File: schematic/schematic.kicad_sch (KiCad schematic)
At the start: 7 parts, among them M1 Stepper_Motor_bipolar, M2 Stepper_Motor_bipolar, U1 module_mpu6050

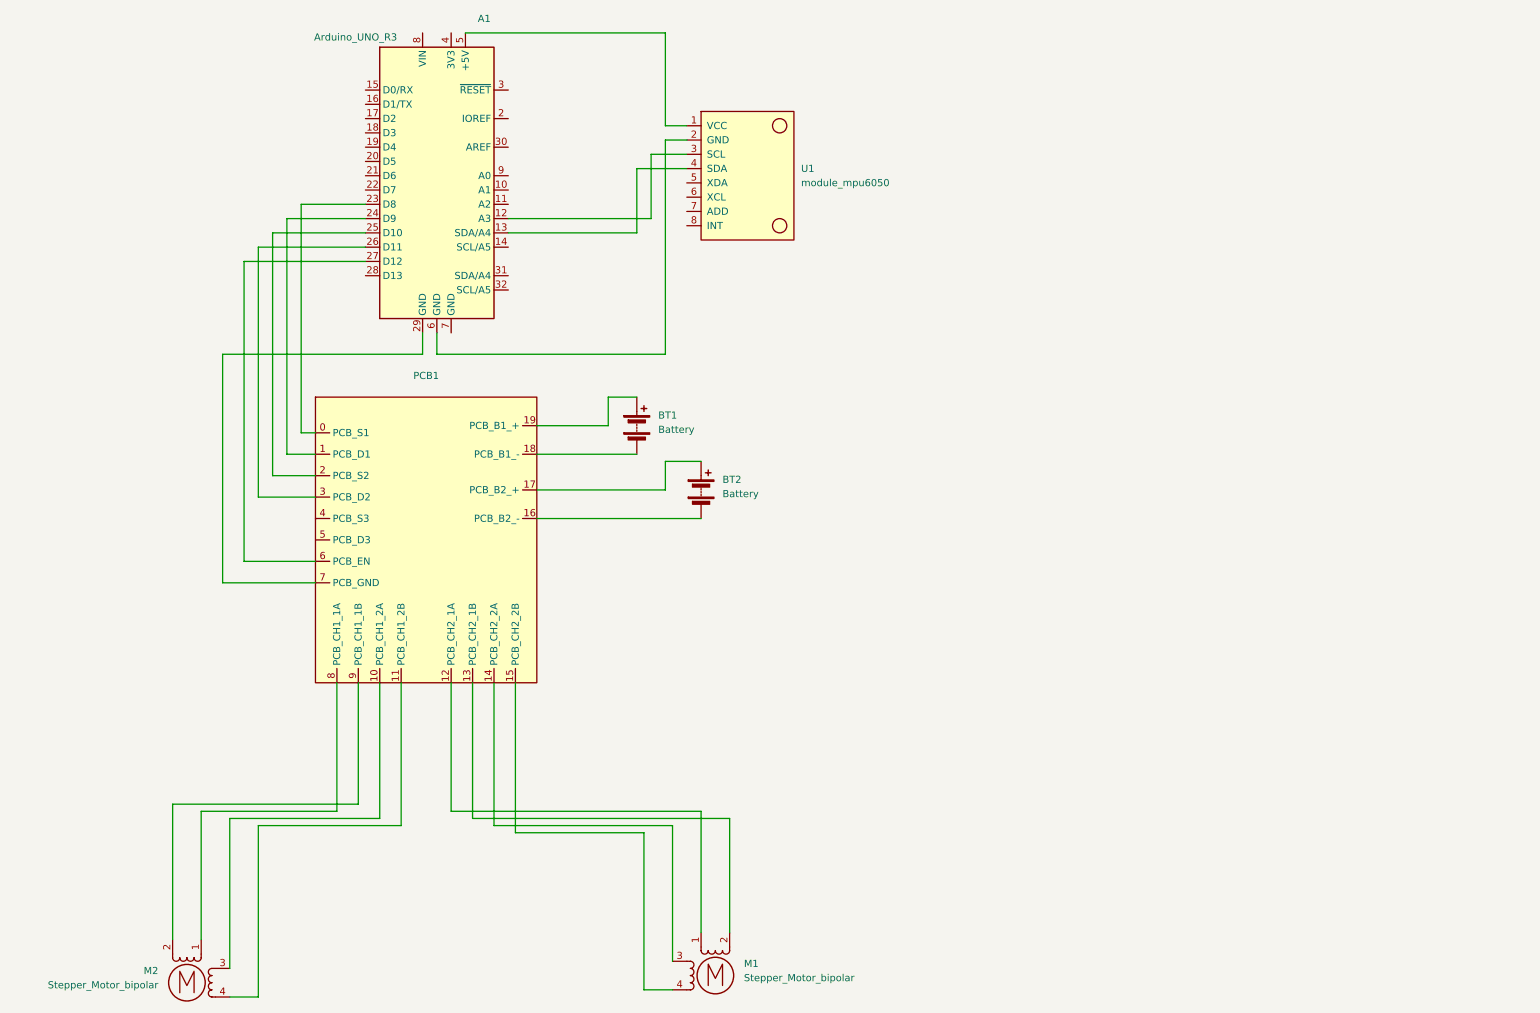
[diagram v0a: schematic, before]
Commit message: Fix MPU6050 pins to Digital pins: D3=SCL, D4=SDA not A3=SCL and A4=SDA
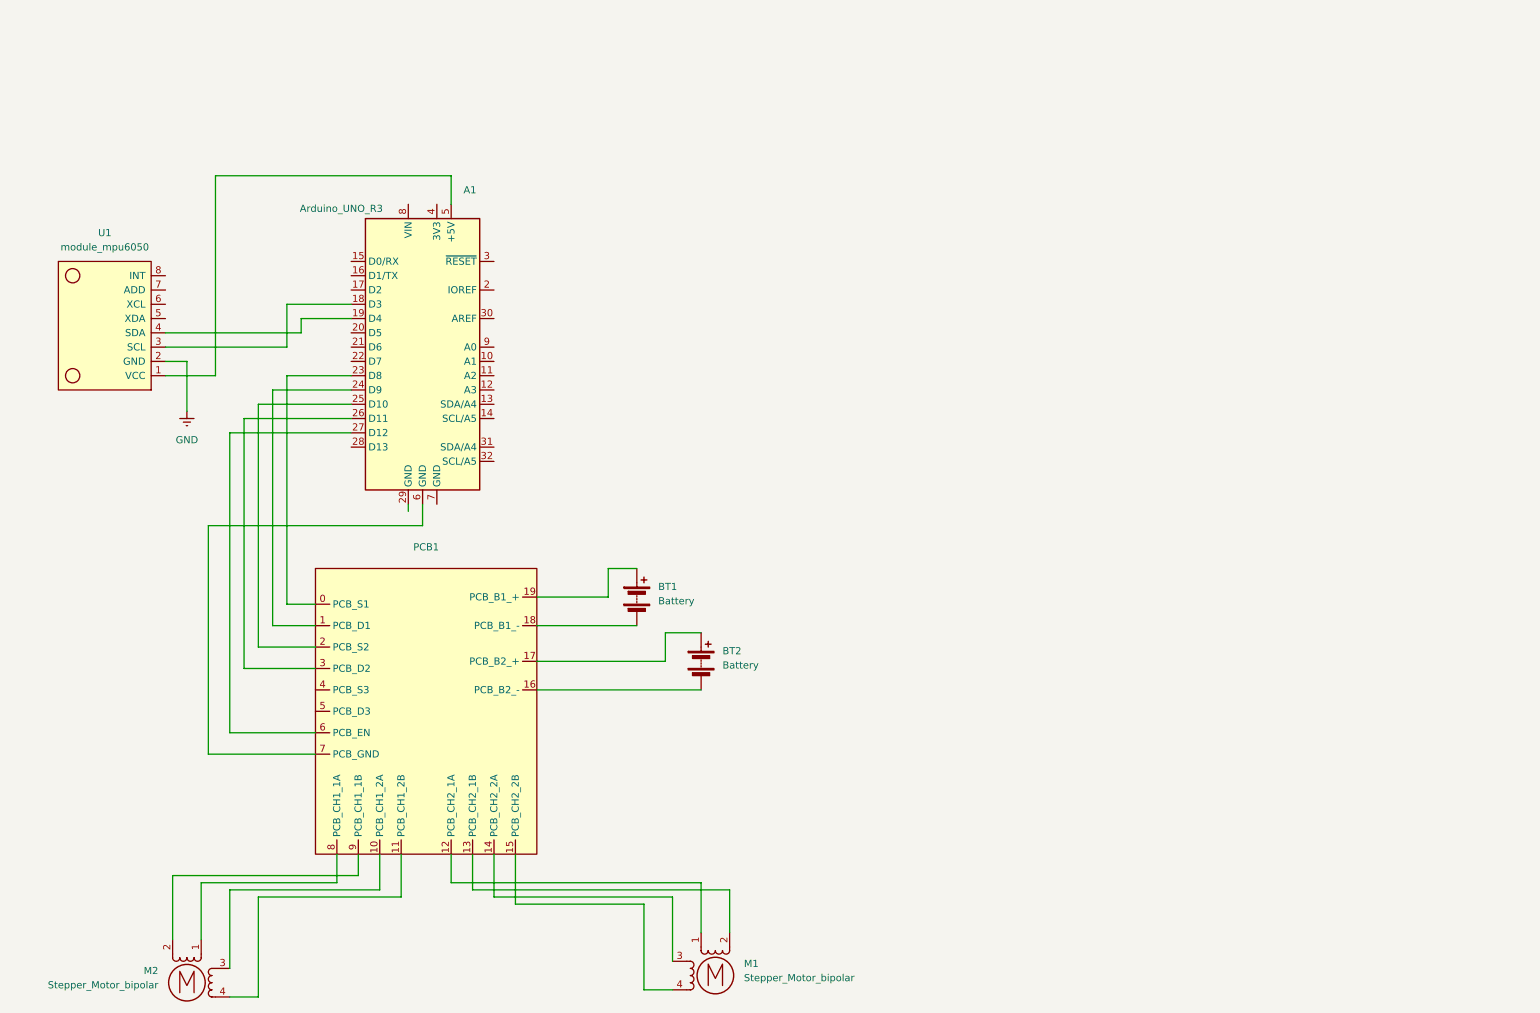
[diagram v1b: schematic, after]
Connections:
- net at PCB1.7 (PCB_GND): now also A1.6 (GND); no longer A1.29 (GND)
- net GND: now reaches U1.2 (GND)
- net GND: no longer A1.6 (GND)
- net at U1.3 (SCL): now also A1.18 (D3); no longer A1.12 (A3)
- net at U1.4 (SDA): now also A1.19 (D4); no longer A1.13 (SDA/A4)
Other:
- moved on the sheet: A1, BT1, BT2, PCB1, U1

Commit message: completed schematic (#19)
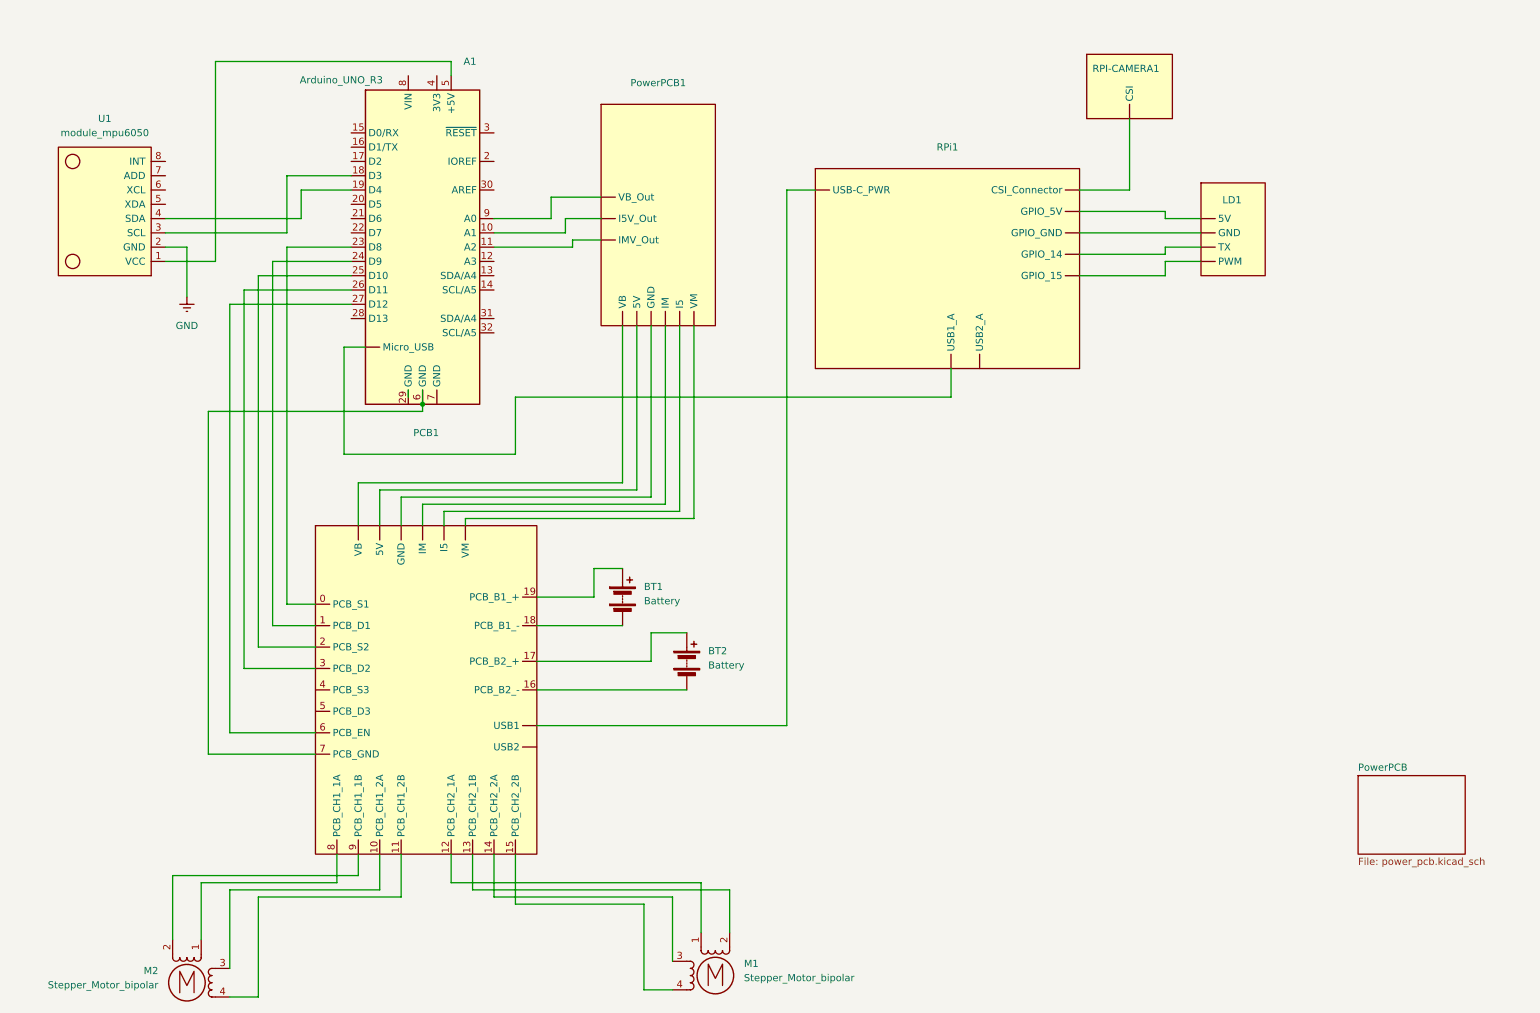
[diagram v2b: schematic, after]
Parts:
- added LD1: ~, symbol BalanceBotSymbolLibrary:LD06
- added PowerPCB1: ~, symbol BalanceBotSymbolLibrary:PowerPCB
- added RPI-CAMERA1: ~, symbol BalanceBotSymbolLibrary:Camera_Module_v2
- added RPi1: ~, symbol BalanceBotSymbolLibrary:RPi4
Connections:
- net at A1.10 (A1): now also PowerPCB1. (VM)
- net at A1.11 (A2): now also PowerPCB1. (VM)
- net at A1.9 (A0): now also PowerPCB1. (VM)
- new net: PCB1. (VM), RPi1. (USB2_A)
- new net: PCB1. (VM), PowerPCB1. (VM) (x6)
- new net: RPI-CAMERA1. (CSI), RPi1. (USB2_A)
- new net: LD1. (TX), RPi1. (USB2_A) (x4)
- new net: A1. (Micro_USB), RPi1. (USB2_A)
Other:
- added sheet PowerPCB (power_pcb.kicad_sch)
- moved on the sheet: BT1, BT2, U1
